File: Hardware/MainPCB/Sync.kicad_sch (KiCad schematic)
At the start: 32 parts, among them Q1 MMBT3904, Q2 MMBT3904, U10 LMH1980, U11 LMH1980, U12 MC74HC86ADTR2G, U13 TS5A3357, U14 74LVC1G3157, U9 74LVC1G3157

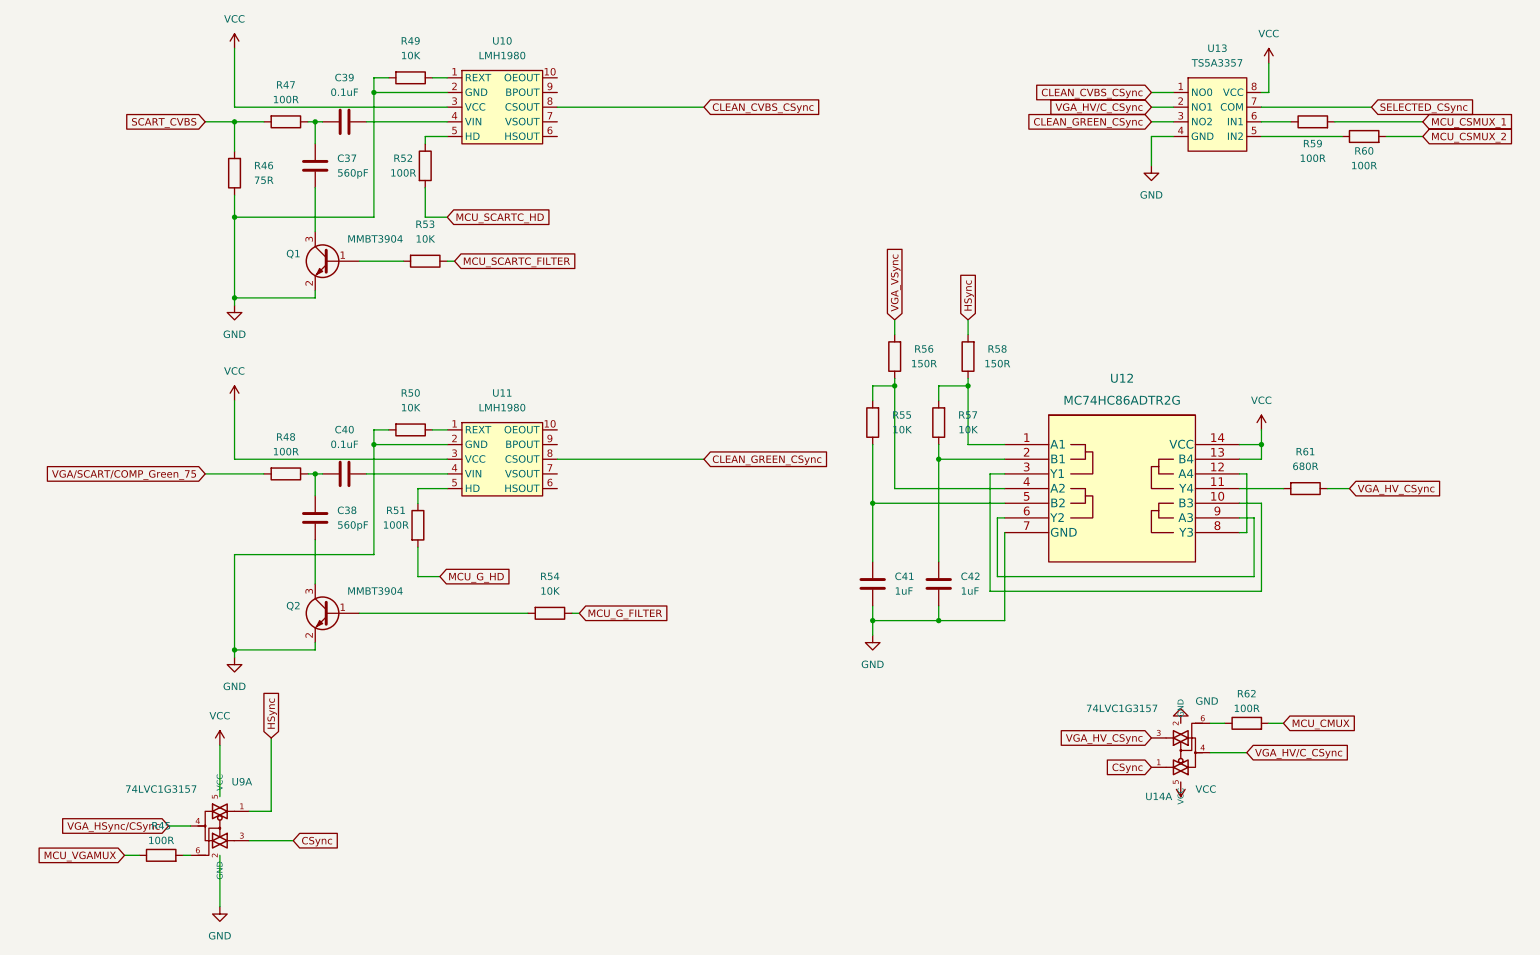
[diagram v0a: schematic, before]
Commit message: Fixed color bending issue; Added diagnostics
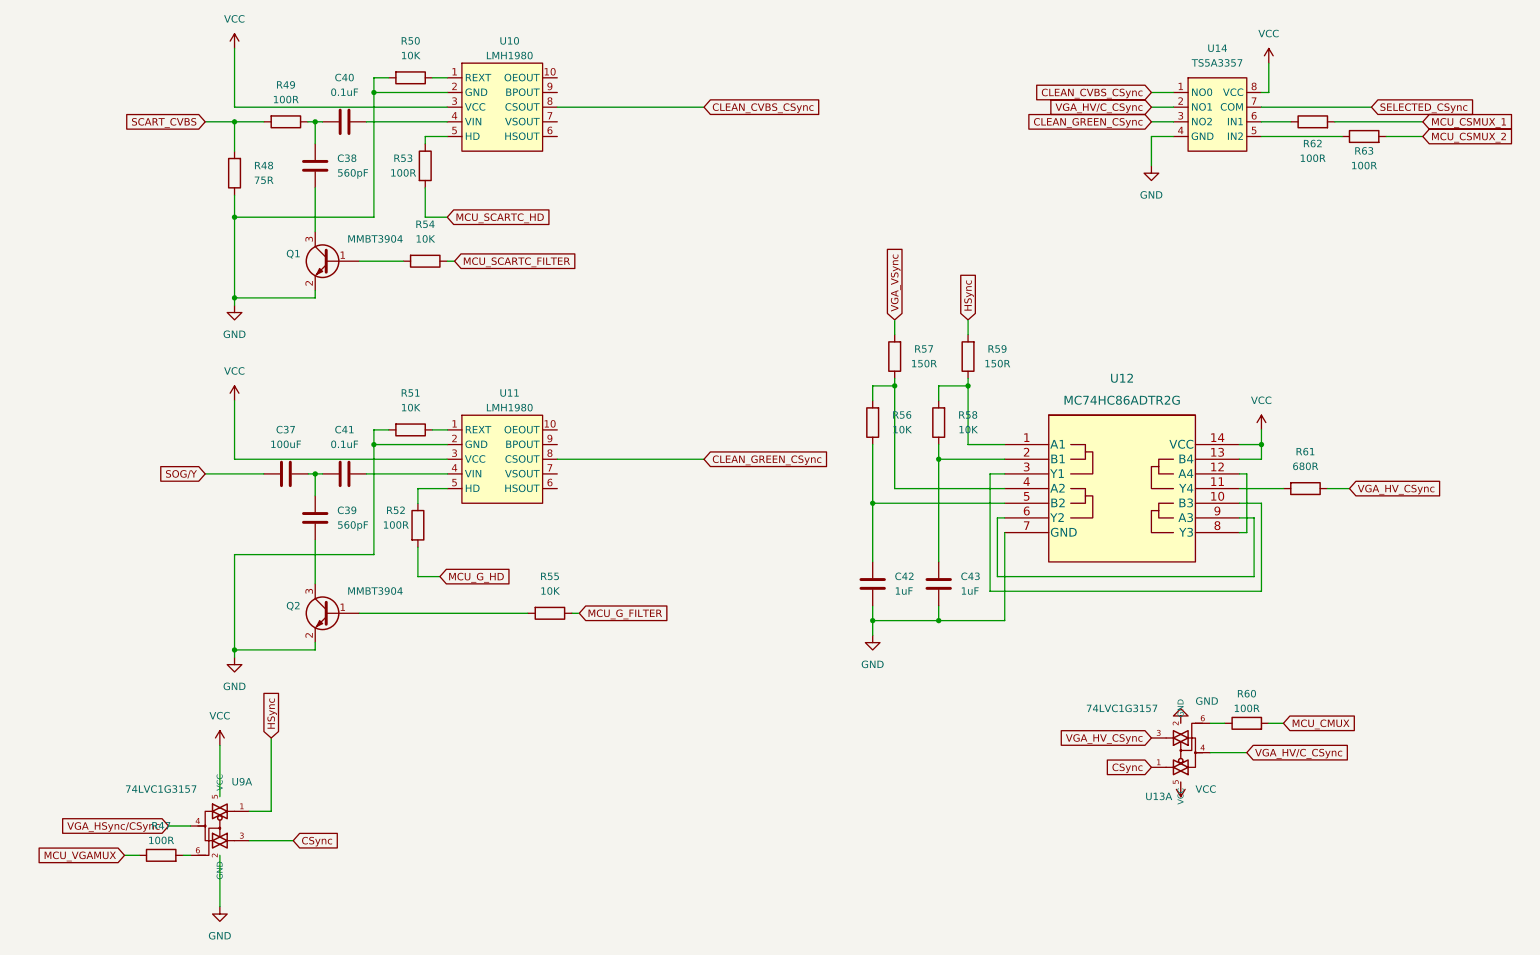
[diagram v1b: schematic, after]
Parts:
- removed R48: 100R, Resistor_SMD:R_0603_1608Metric, symbol Device:R
- added C37: 100uF, Capacitor_SMD:C_0805_2012Metric, symbol Device:C
- R47: renamed from R45; footprint Resistor_SMD:R_0603_1608Metric -> RT5XP-EXP:R_0603; symbol Device:R -> RT5XP_EXP:R
- R48: renamed from R46; footprint Resistor_SMD:R_0603_1608Metric -> RT5XP-EXP:R_0603; symbol Device:R -> RT5XP_EXP:R
- R49: renamed from R47; footprint Resistor_SMD:R_0603_1608Metric -> RT5XP-EXP:R_0603; symbol Device:R -> RT5XP_EXP:R
- R50: renamed from R49; footprint Resistor_SMD:R_0603_1608Metric -> RT5XP-EXP:R_0603; symbol Device:R -> RT5XP_EXP:R
- R51: renamed from R50; footprint Resistor_SMD:R_0603_1608Metric -> RT5XP-EXP:R_0603; symbol Device:R -> RT5XP_EXP:R
- R52: renamed from R51; footprint Resistor_SMD:R_0603_1608Metric -> RT5XP-EXP:R_0603; symbol Device:R -> RT5XP_EXP:R
- R53: renamed from R52; footprint Resistor_SMD:R_0603_1608Metric -> RT5XP-EXP:R_0603; symbol Device:R -> RT5XP_EXP:R
- R54: renamed from R53; footprint Resistor_SMD:R_0603_1608Metric -> RT5XP-EXP:R_0603; symbol Device:R -> RT5XP_EXP:R
- R55: renamed from R54; footprint Resistor_SMD:R_0603_1608Metric -> RT5XP-EXP:R_0603; symbol Device:R -> RT5XP_EXP:R
- R56: renamed from R55; footprint Resistor_SMD:R_0603_1608Metric -> RT5XP-EXP:R_0603; symbol Device:R -> RT5XP_EXP:R
- R57: renamed from R56; footprint Resistor_SMD:R_0603_1608Metric -> RT5XP-EXP:R_0603; symbol Device:R -> RT5XP_EXP:R
- R58: renamed from R57; footprint Resistor_SMD:R_0603_1608Metric -> RT5XP-EXP:R_0603; symbol Device:R -> RT5XP_EXP:R
- R59: renamed from R58; footprint Resistor_SMD:R_0603_1608Metric -> RT5XP-EXP:R_0603; symbol Device:R -> RT5XP_EXP:R
- R60: renamed from R62; footprint Resistor_SMD:R_0603_1608Metric -> RT5XP-EXP:R_0603; symbol Device:R -> RT5XP_EXP:R
- R61: footprint Resistor_SMD:R_0603_1608Metric -> RT5XP-EXP:R_0603; symbol Device:R -> RT5XP_EXP:R
- R62: renamed from R59; footprint Resistor_SMD:R_0603_1608Metric -> RT5XP-EXP:R_0603; symbol Device:R -> RT5XP_EXP:R
- R63: renamed from R60; footprint Resistor_SMD:R_0603_1608Metric -> RT5XP-EXP:R_0603; symbol Device:R -> RT5XP_EXP:R
- U10, U11: footprint Package_SO:VSSOP-10_3x3mm_P0.5mm -> RT5XP-EXP:VSSOP-10_3x3mm_P0.5mm; symbol AE:LMH1980 -> RT5XP_EXP:LMH1980
- renumbered C37 to C38, C38 to C39, C39 to C40, C40 to C41, C41 to C42, C42 to C43, U14 to U13, U13 to U14
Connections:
- net at C39.2, C41.1: now also C37.2
- new net SOG/Y: C37.1
